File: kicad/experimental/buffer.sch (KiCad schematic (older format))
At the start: 37 parts, among them J1 PWR_IN, J2 SIG_IN, J3 SIG_OUT, U1 OPA2197, U2 OPA2197

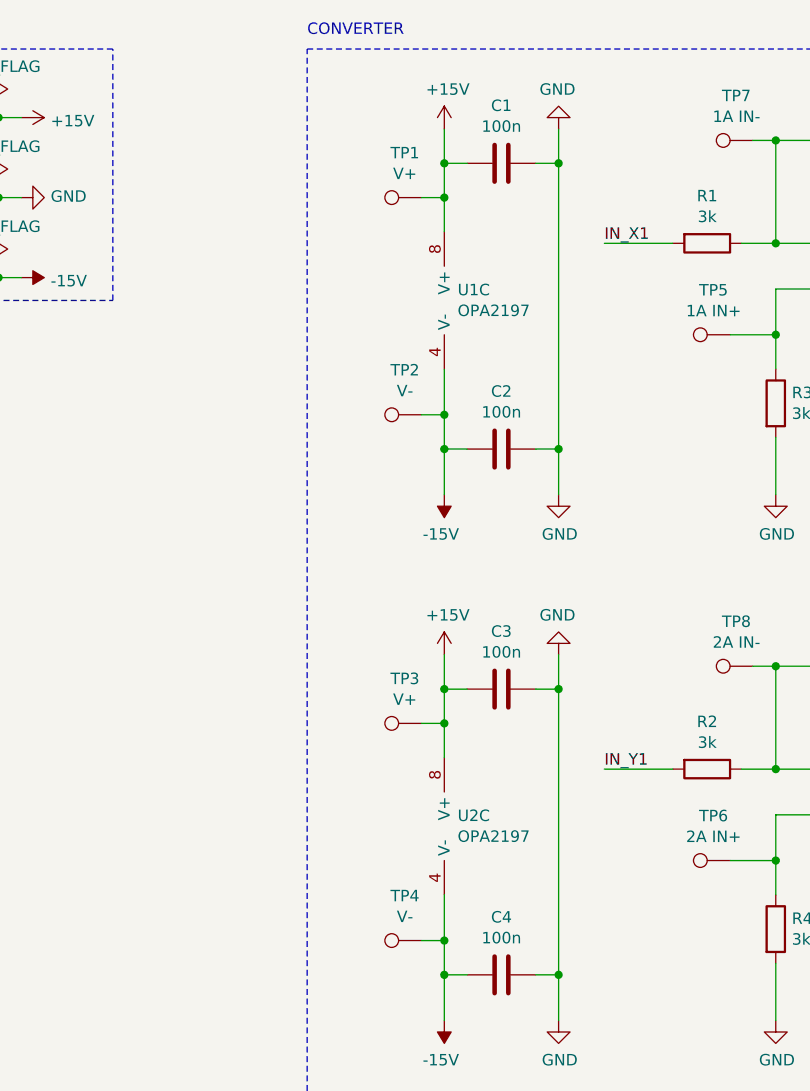
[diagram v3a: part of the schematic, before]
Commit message: designed pcb for experimental buffer board
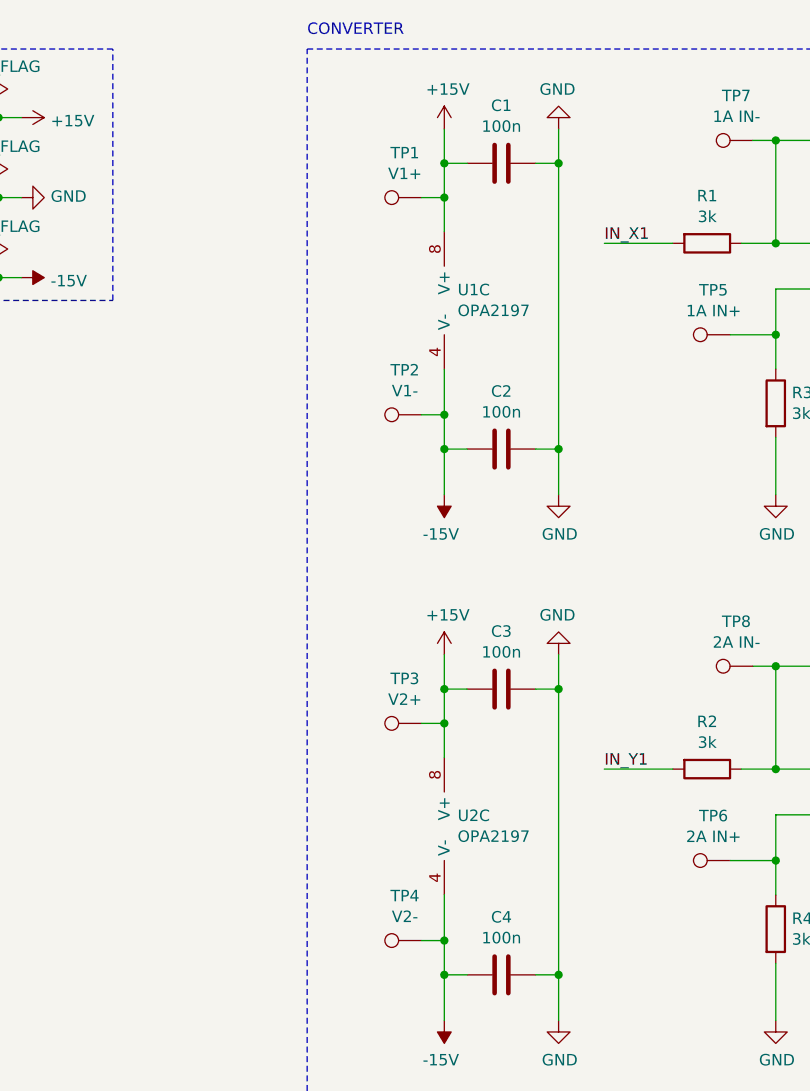
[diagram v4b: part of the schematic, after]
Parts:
- TP1: value V+ -> V1+; footprint TestPoint:TestPoint_THTPad_1.0x1.0mm_Drill0.5mm -> TestPoint:TestPoint_THTPad_D1.0mm_Drill0.5mm
- TP10, TP11, TP12, TP13, TP14, TP15, TP16, TP5, TP6, TP7, TP8, TP9: footprint TestPoint:TestPoint_THTPad_1.0x1.0mm_Drill0.5mm -> TestPoint:TestPoint_THTPad_D1.0mm_Drill0.5mm
- TP2: value V- -> V1-; footprint TestPoint:TestPoint_THTPad_1.0x1.0mm_Drill0.5mm -> TestPoint:TestPoint_THTPad_D1.0mm_Drill0.5mm
- TP3: value V+ -> V2+; footprint TestPoint:TestPoint_THTPad_1.0x1.0mm_Drill0.5mm -> TestPoint:TestPoint_THTPad_D1.0mm_Drill0.5mm
- TP4: value V- -> V2-; footprint TestPoint:TestPoint_THTPad_1.0x1.0mm_Drill0.5mm -> TestPoint:TestPoint_THTPad_D1.0mm_Drill0.5mm
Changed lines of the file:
@@
 P 3500 1650
 F 0 "TP1" V 3695 1722 50  0000 C CNN
-F 1 "V+" V 3604 1722 50  0000 C CNN
-F 2 "TestPoint:TestPoint_THTPad_1.0x1.0mm_Drill0.5mm" H 3700 1650 50  0001 C CNN
+F 1 "V1+" V 3604 1722 50  0000 C CNN
+F 2 "TestPoint:TestPoint_THTPad_D1.0mm_Drill0.5mm" H 3700 1650 50  0001 C CNN
 F 3 "~" H 3700 1650 50  0001 C CNN
 	1    3500 1650
@@
 P 3500 2600
 F 0 "TP2" V 3695 2672 50  0000 C CNN
-F 1 "V-" V 3604 2672 50  0000 C CNN
-F 2 "TestPoint:TestPoint_THTPad_1.0x1.0mm_Drill0.5mm" H 3700 2600 50  0001 C CNN
+F 1 "V1-" V 3604 2672 50  0000 C CNN
+F 2 "TestPoint:TestPoint_THTPad_D1.0mm_Drill0.5mm" H 3700 2600 50  0001 C CNN
 F 3 "~" H 3700 2600 50  0001 C CNN
 	1    3500 2600
@@
 F 0 "TP5" V 5045 2322 50  0000 C CNN
 F 1 "1A IN+" V 4954 2322 50  0000 C CNN
-F 2 "TestPoint:TestPoint_THTPad_1.0x1.0mm_Drill0.5mm" H 5050 2250 50  0001 C CNN
+F 2 "TestPoint:TestPoint_THTPad_D1.0mm_Drill0.5mm" H 5050 2250 50  0001 C CNN
 F 3 "~" H 5050 2250 50  0001 C CNN
 	1    4850 2250
@@
 F 0 "TP7" V 5145 1472 50  0000 C CNN
 F 1 "1A IN-" V 5054 1472 50  0000 C CNN
-F 2 "TestPoint:TestPoint_THTPad_1.0x1.0mm_Drill0.5mm" H 5150 1400 50  0001 C CNN
+F 2 "TestPoint:TestPoint_THTPad_D1.0mm_Drill0.5mm" H 5150 1400 50  0001 C CNN
 F 3 "~" H 5150 1400 50  0001 C CNN
 	1    4950 1400
@@
 F 0 "TP9" V 6250 1400 50  0000 L CNN
 F 1 "1A OUT" V 6150 1400 50  0000 L CNN
-F 2 "TestPoint:TestPoint_THTPad_1.0x1.0mm_Drill0.5mm" H 6250 1400 50  0001 C CNN
+F 2 "TestPoint:TestPoint_THTPad_D1.0mm_Drill0.5mm" H 6250 1400 50  0001 C CNN
 F 3 "~" H 6250 1400 50  0001 C CNN
 	1    6050 1400
@@
 F 0 "TP11" V 7195 2322 50  0000 C CNN
 F 1 "1B IN+" V 7104 2322 50  0000 C CNN
-F 2 "TestPoint:TestPoint_THTPad_1.0x1.0mm_Drill0.5mm" H 7200 2250 50  0001 C CNN
+F 2 "TestPoint:TestPoint_THTPad_D1.0mm_Drill0.5mm" H 7200 2250 50  0001 C CNN
 F 3 "~" H 7200 2250 50  0001 C CNN
 	1    7000 2250
@@
 F 0 "TP13" V 7295 1472 50  0000 C CNN
 F 1 "1B IN-" V 7204 1472 50  0000 C CNN
-F 2 "TestPoint:TestPoint_THTPad_1.0x1.0mm_Drill0.5mm" H 7300 1400 50  0001 C CNN
+F 2 "TestPoint:TestPoint_THTPad_D1.0mm_Drill0.5mm" H 7300 1400 50  0001 C CNN
 F 3 "~" H 7300 1400 50  0001 C CNN
 	1    7100 1400
@@
 F 0 "TP15" V 8400 1400 50  0000 L CNN
 F 1 "1B OUT" V 8300 1400 50  0000 L CNN
-F 2 "TestPoint:TestPoint_THTPad_1.0x1.0mm_Drill0.5mm" H 8400 1400 50  0001 C CNN
+F 2 "TestPoint:TestPoint_THTPad_D1.0mm_Drill0.5mm" H 8400 1400 50  0001 C CNN
 F 3 "~" H 8400 1400 50  0001 C CNN
 	1    8200 1400
@@
 P 3500 3950
 F 0 "TP3" V 3695 4022 50  0000 C CNN
-F 1 "V+" V 3604 4022 50  0000 C CNN
-F 2 "TestPoint:TestPoint_THTPad_1.0x1.0mm_Drill0.5mm" H 3700 3950 50  0001 C CNN
+F 1 "V2+" V 3604 4022 50  0000 C CNN
+F 2 "TestPoint:TestPoint_THTPad_D1.0mm_Drill0.5mm" H 3700 3950 50  0001 C CNN
 F 3 "~" H 3700 3950 50  0001 C CNN
 	1    3500 3950
@@
 P 3500 4900
 F 0 "TP4" V 3695 4972 50  0000 C CNN
-F 1 "V-" V 3604 4972 50  0000 C CNN
-F 2 "TestPoint:TestPoint_THTPad_1.0x1.0mm_Drill0.5mm" H 3700 4900 50  0001 C CNN
+F 1 "V2-" V 3604 4972 50  0000 C CNN
+F 2 "TestPoint:TestPoint_THTPad_D1.0mm_Drill0.5mm" H 3700 4900 50  0001 C CNN
 F 3 "~" H 3700 4900 50  0001 C CNN
 	1    3500 4900
@@
 F 0 "TP6" V 5045 4622 50  0000 C CNN
 F 1 "2A IN+" V 4954 4622 50  0000 C CNN
-F 2 "TestPoint:TestPoint_THTPad_1.0x1.0mm_Drill0.5mm" H 5050 4550 50  0001 C CNN
+F 2 "TestPoint:TestPoint_THTPad_D1.0mm_Drill0.5mm" H 5050 4550 50  0001 C CNN
 F 3 "~" H 5050 4550 50  0001 C CNN
 	1    4850 4550
@@
 F 0 "TP8" V 5145 3772 50  0000 C CNN
 F 1 "2A IN-" V 5054 3772 50  0000 C CNN
-F 2 "TestPoint:TestPoint_THTPad_1.0x1.0mm_Drill0.5mm" H 5150 3700 50  0001 C CNN
+F 2 "TestPoint:TestPoint_THTPad_D1.0mm_Drill0.5mm" H 5150 3700 50  0001 C CNN
 F 3 "~" H 5150 3700 50  0001 C CNN
 	1    4950 3700
@@
 F 0 "TP10" V 6250 3700 50  0000 L CNN
 F 1 "2A OUT" V 6150 3700 50  0000 L CNN
-F 2 "TestPoint:TestPoint_THTPad_1.0x1.0mm_Drill0.5mm" H 6250 3700 50  0001 C CNN
+F 2 "TestPoint:TestPoint_THTPad_D1.0mm_Drill0.5mm" H 6250 3700 50  0001 C CNN
 F 3 "~" H 6250 3700 50  0001 C CNN
 	1    6050 3700
@@
 F 0 "TP12" V 7195 4622 50  0000 C CNN
 F 1 "2B IN+" V 7104 4622 50  0000 C CNN
-F 2 "TestPoint:TestPoint_THTPad_1.0x1.0mm_Drill0.5mm" H 7200 4550 50  0001 C CNN
+F 2 "TestPoint:TestPoint_THTPad_D1.0mm_Drill0.5mm" H 7200 4550 50  0001 C CNN
 F 3 "~" H 7200 4550 50  0001 C CNN
 	1    7000 4550
@@
 F 0 "TP14" V 7295 3772 50  0000 C CNN
 F 1 "2B IN-" V 7204 3772 50  0000 C CNN
-F 2 "TestPoint:TestPoint_THTPad_1.0x1.0mm_Drill0.5mm" H 7300 3700 50  0001 C CNN
+F 2 "TestPoint:TestPoint_THTPad_D1.0mm_Drill0.5mm" H 7300 3700 50  0001 C CNN
 F 3 "~" H 7300 3700 50  0001 C CNN
 	1    7100 3700
@@
 F 0 "TP16" V 8400 3700 50  0000 L CNN
 F 1 "2B OUT" V 8300 3700 50  0000 L CNN
-F 2 "TestPoint:TestPoint_THTPad_1.0x1.0mm_Drill0.5mm" H 8400 3700 50  0001 C CNN
+F 2 "TestPoint:TestPoint_THTPad_D1.0mm_Drill0.5mm" H 8400 3700 50  0001 C CNN
 F 3 "~" H 8400 3700 50  0001 C CNN
 	1    8200 3700
